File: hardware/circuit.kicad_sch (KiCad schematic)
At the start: 3 parts

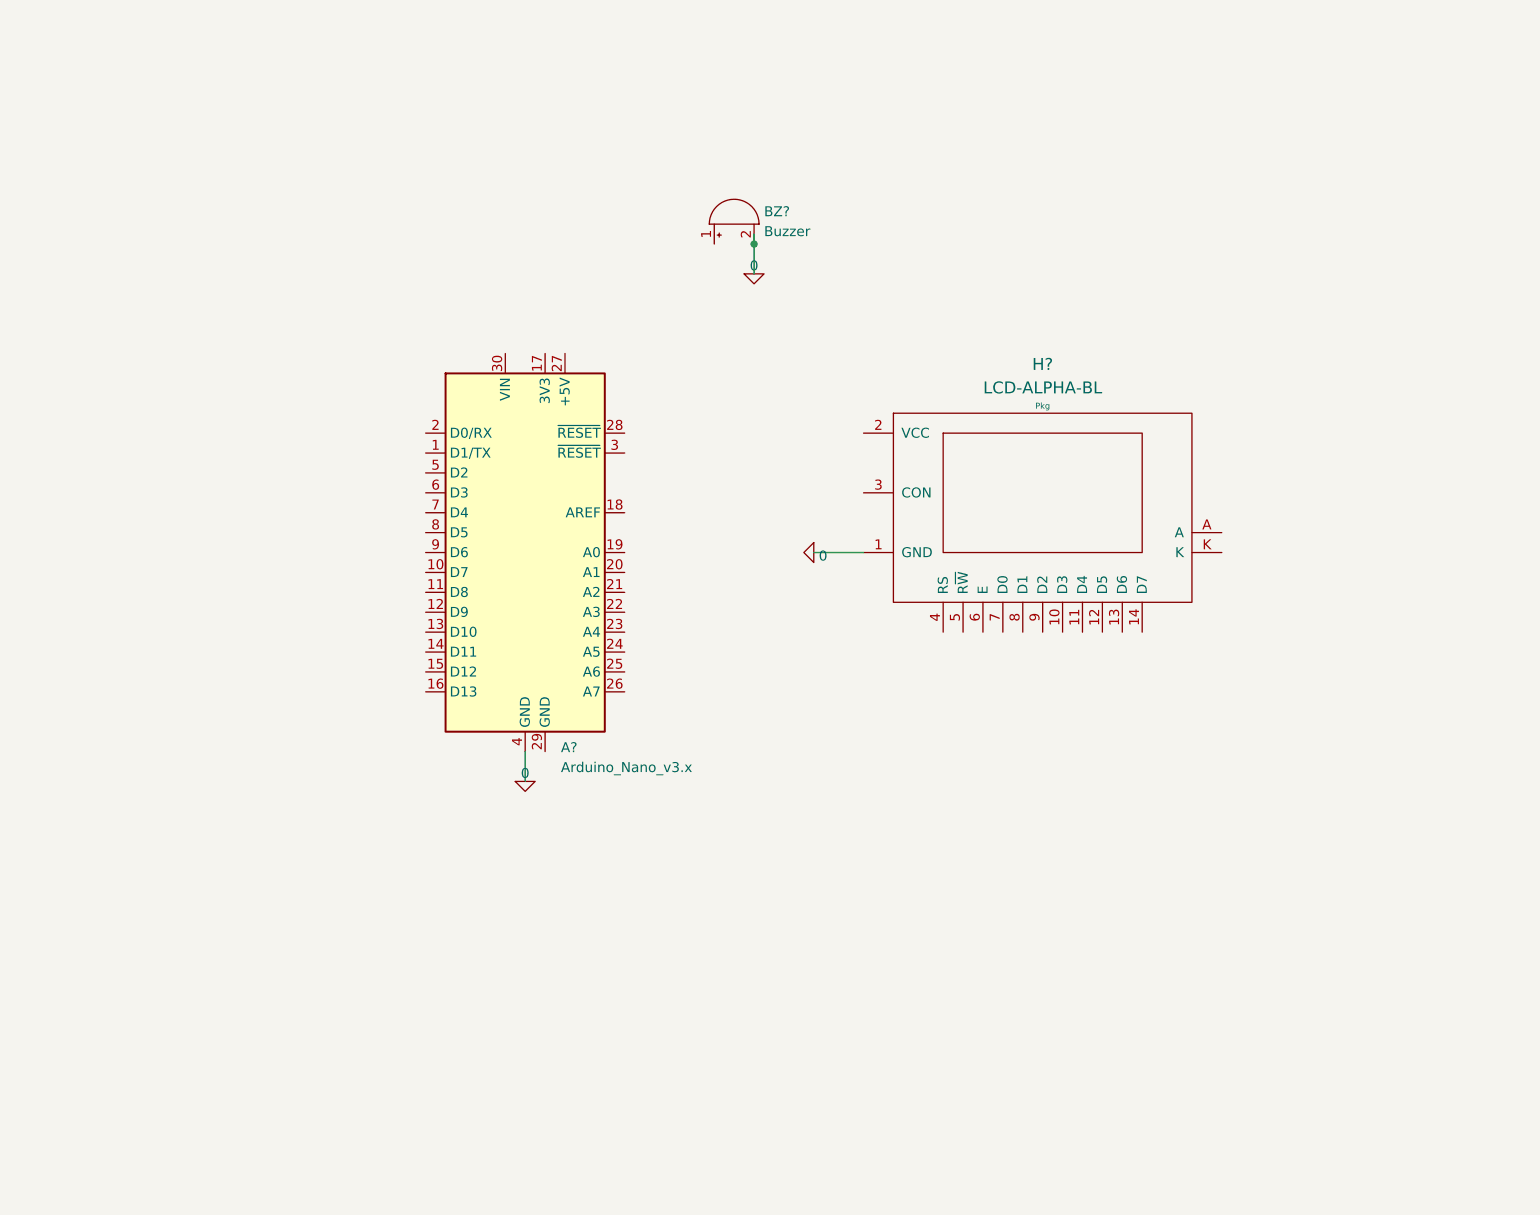
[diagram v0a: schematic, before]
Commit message: Added(guiMessage): generic lcd gui message functions
  Moved src/system/* to /, corrected some linting errors.
  Made some minor changes to hardware schematic.
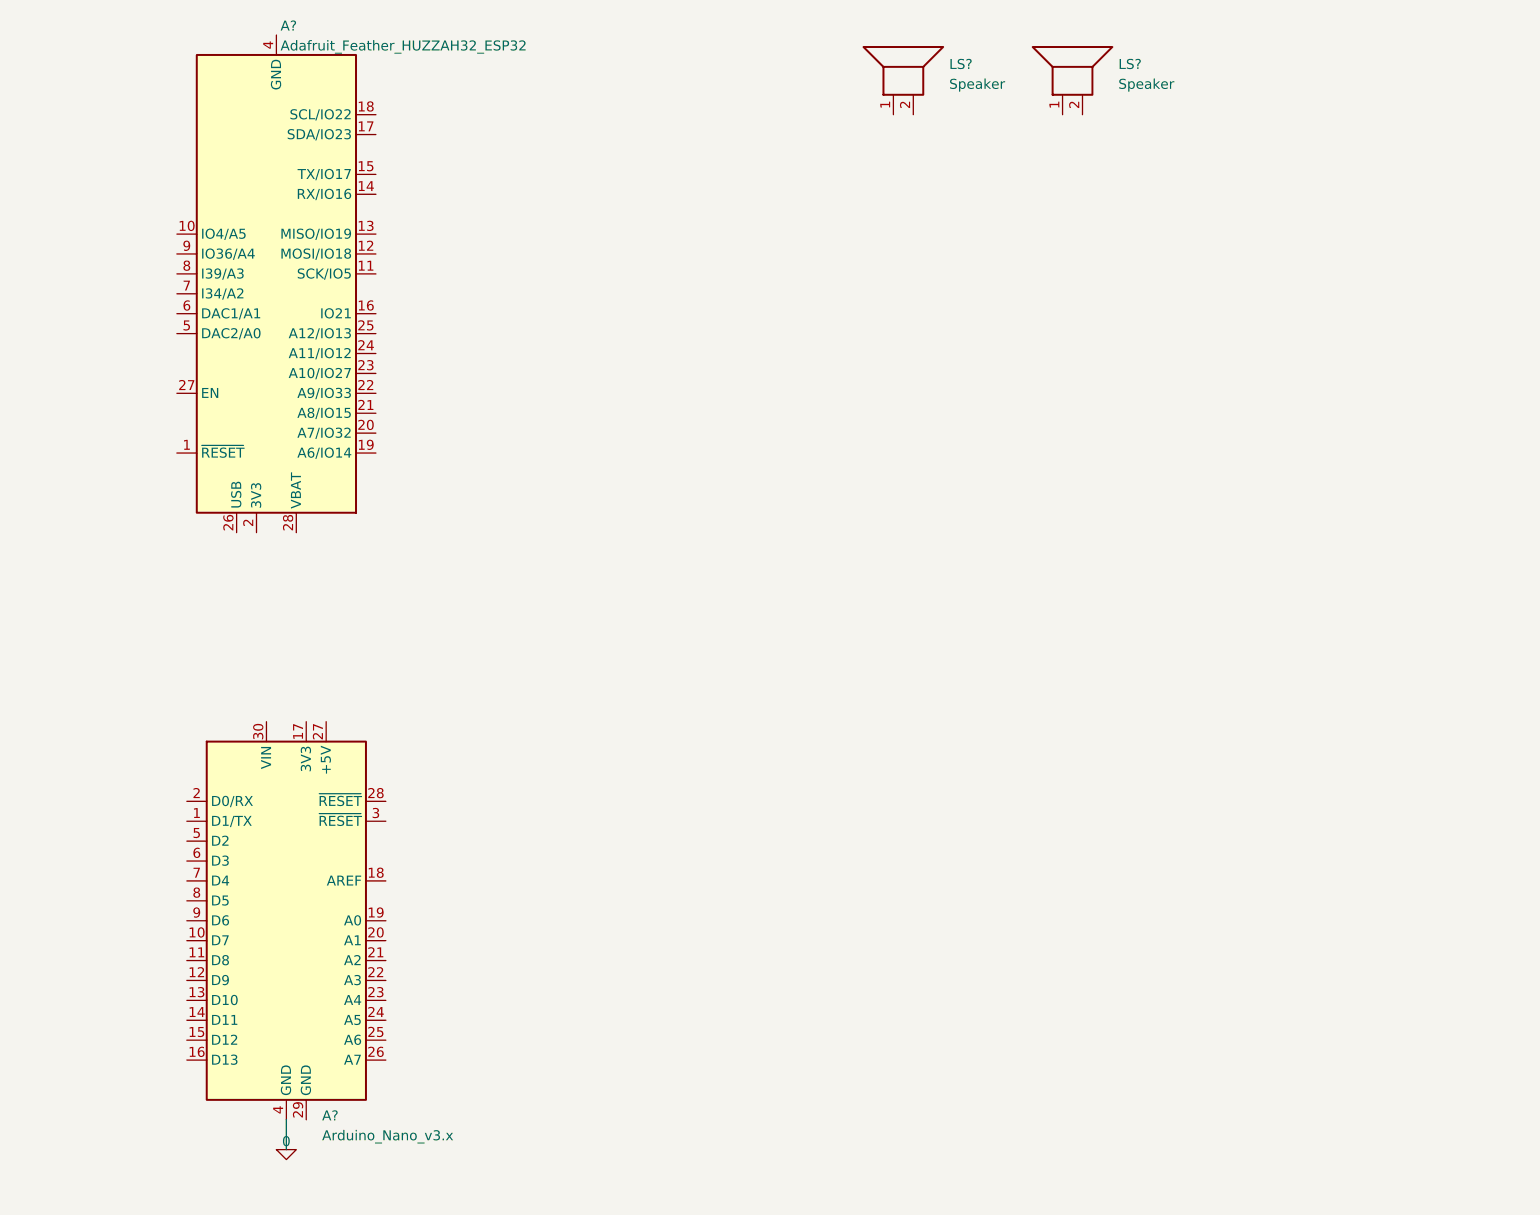
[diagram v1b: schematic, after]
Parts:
- removed BZ?: Buzzer, symbol Device:Buzzer
- removed H?: LCD-ALPHA-BL, Pkg, symbol display:LCD-ALPHA-BL
- added A?: Adafruit_Feather_HUZZAH32_ESP32, Module:Adafruit_Feather, symbol MCU_Module:Adafruit_Feather_HUZZAH32_ESP32
- added LS? (x2): Speaker, symbol Device:Speaker
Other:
- moved on the sheet: A?
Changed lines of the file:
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@@
 (kicad_sch (version 20211123) (generator eeschema)
   (paper "A4")
-  (junction (at 121.92 54.61) (diameter 0) (color 0 0 0 0)
-  )
-  (wire (pts (xy 121.92 53.34) (xy 121.92 54.61))
+  (wire (pts (xy 62.23 166.37) (xy 62.23 170.18))
     (stroke (width 0) (type default) (color 0 0 0 0))
   )
-  (wire (pts (xy 129.54 93.98) (xy 135.89 93.98))
-    (stroke (width 0) (type default) (color 0 0 0 0))
-  )
-  (wire (pts (xy 92.71 119.38) (xy 92.71 123.19))
-    (stroke (width 0) (type default) (color 0 0 0 0))
-  )
-  (wire (pts (xy 121.92 58.42) (xy 121.92 54.61))
-    (stroke (width 0) (type default) (color 0 0 0 0))
-  )
-  (symbol (lib_id "pspice:0") (at 129.54 93.98 270) (unit 1)
+  (symbol (lib_id "pspice:0") (at 62.23 170.18 0) (unit 1)
     (in_bom yes) (on_board yes) (fields_autoplaced)
-    (property "Reference" "#GND?" (id 0) (at 127 93.98 0)
+    (property "Reference" "#GND?" (id 0) (at 62.23 172.72 0)
       (effects (font (size 1.27 1.27)) hide)
     )
-    (property "Value" "0" (id 1) (at 130.175 94.4138 90)
-      (effects (font (size 1.27 1.27)) (justify left))
-    )
-    (property "Footprint" "" (id 2) (at 129.54 93.98 0)
+    (property "Value" "0" (id 1) (at 62.23 169.1442 0))
+    (property "Footprint" "" (id 2) (at 62.23 170.18 0)
       (effects (font (size 1.27 1.27)) hide)
     )
-    (property "Datasheet" "~" (id 3) (at 129.54 93.98 0)
+    (property "Datasheet" "~" (id 3) (at 62.23 170.18 0)
       (effects (font (size 1.27 1.27)) hide)
     )
     (pin "1")
   )
-  (symbol (lib_id "Device:Buzzer") (at 119.38 52.07 90) (unit 1)
+  (symbol (lib_id "MCU_Module:Adafruit_Feather_HUZZAH32_ESP32") (at 60.96 60.96 180) (unit 1)
     (in_bom yes) (on_board yes) (fields_autoplaced)
-    (property "Reference" "BZ?" (id 0) (at 123.19 50.4733 90)
+    (property "Reference" "A?" (id 0) (at 61.4806 26.7802 0)
       (effects (font (size 1.27 1.27)) (justify right))
     )
-    (property "Value" "Buzzer" (id 1) (at 123.19 53.0102 90)
+    (property "Value" "Adafruit_Feather_HUZZAH32_ESP32" (id 1) (at 61.4806 29.3171 0)
       (effects (font (size 1.27 1.27)) (justify right))
     )
-    (property "Footprint" "" (id 2) (at 116.84 52.705 90)
+    (property "Footprint" "Module:Adafruit_Feather" (id 2) (at 58.42 26.67 0)
+      (effects (font (size 1.27 1.27)) (justify left) hide)
+    )
+    (property "Datasheet" "https://cdn-learn.adafruit.com/downloads/pdf/adafruit-huzzah32-esp32-feather.pdf" (id 3) (at 60.96 30.48 0)
       (effects (font (size 1.27 1.27)) hide)
     )
-    (property "Datasheet" "~" (id 3) (at 116.84 52.705 90)
-      (effects (font (size 1.27 1.27)) hide)
-    )
-    (pin "1")
-    (pin "2")
-  )
-  (symbol (lib_id "pspice:0") (at 92.71 123.19 0) (unit 1)
-    (in_bom yes) (on_board yes) (fields_autoplaced)
-    (property "Reference" "#GND?" (id 0) (at 92.71 125.73 0)
-      (effects (font (size 1.27 1.27)) hide)
-    )
-    (property "Value" "0" (id 1) (at 92.71 122.1542 0))
-    (property "Footprint" "" (id 2) (at 92.71 123.19 0)
-      (effects (font (size 1.27 1.27)) hide)
-    )
-    (property "Datasheet" "~" (id 3) (at 92.71 123.19 0)
-      (effects (font (size 1.27 1.27)) hide)
-    )
-    (pin "1")
-  )
-  (symbol (lib_id "pspice:0") (at 121.92 58.42 0) (unit 1)
-    (in_bom yes) (on_board yes) (fields_autoplaced)
-    (property "Reference" "#GND?" (id 0) (at 121.92 60.96 0)
-      (effects (font (size 1.27 1.27)) hide)
-    )
-    (property "Value" "0" (id 1) (at 121.92 57.3842 0))
-    (property "Footprint" "" (id 2) (at 121.92 58.42 0)
-      (effects (font (size 1.27 1.27)) hide)
-    )
-    (property "Datasheet" "~" (id 3) (at 121.92 58.42 0)
-      (effects (font (size 1.27 1.27)) hide)
-    )
-    (pin "1")
-  )
-  (symbol (lib_id "display:LCD-ALPHA-BL") (at 158.75 86.36 0) (unit 1)
-    (in_bom yes) (on_board yes) (fields_autoplaced)
-    (property "Reference" "H?" (id 0) (at 158.75 69.9717 0)
-      (effects (font (size 1.524 1.524)))
-    )
-    (property "Value" "LCD-ALPHA-BL" (id 1) (at 158.75 72.9651 0)
-      (effects (font (size 1.524 1.524)))
-    )
-    (property "Footprint" "Pkg" (id 2) (at 158.75 75.2737 0)
-      (effects (font (size 0.762 0.762)))
-    )
-    (property "Datasheet" "" (id 3) (at 158.75 86.36 0))
     (pin "1")
     (pin "10")
@@
     (pin "13")
     (pin "14")
+    (pin "15")
+    (pin "16")
+    (pin "17")
+    (pin "18")
+    (pin "19")
     (pin "2")
+    (pin "20")
+    (pin "21")
+    (pin "22")
+    (pin "23")
+    (pin "24")
+    (pin "25")
+    (pin "26")
+    (pin "27")
+    (pin "28")
     (pin "3")
     (pin "4")
@@
     (pin "8")
     (pin "9")
-    (pin "A")
-    (pin "K")
   )
-  (symbol (lib_id "MCU_Module:Arduino_Nano_v3.x") (at 92.71 93.98 0) (unit 1)
+  (symbol (lib_id "Device:Speaker") (at 161.29 33.02 90) (unit 1)
     (in_bom yes) (on_board yes) (fields_autoplaced)
-    (property "Reference" "A?" (id 0) (at 97.2694 118.8704 0)
+    (property "Reference" "LS?" (id 0) (at 168.402 31.6773 90)
+      (effects (font (size 1.27 1.27)) (justify right))
+    )
+    (property "Value" "Speaker" (id 1) (at 168.402 34.2142 90)
+      (effects (font (size 1.27 1.27)) (justify right))
+    )
+    (property "Footprint" "" (id 2) (at 166.37 33.02 0)
+      (effects (font (size 1.27 1.27)) hide)
+    )
+    (property "Datasheet" "~" (id 3) (at 162.56 33.274 0)
+      (effects (font (size 1.27 1.27)) hide)
+    )
+    (pin "1")
+    (pin "2")
+  )
+  (symbol (lib_id "MCU_Module:Arduino_Nano_v3.x") (at 62.23 140.97 0) (unit 1)
+    (in_bom yes) (on_board yes) (fields_autoplaced)
+    (property "Reference" "A?" (id 0) (at 66.7894 165.8604 0)
       (effects (font (size 1.27 1.27)) (justify left))
     )
-    (property "Value" "Arduino_Nano_v3.x" (id 1) (at 97.2694 121.4073 0)
+    (property "Value" "Arduino_Nano_v3.x" (id 1) (at 66.7894 168.3973 0)
       (effects (font (size 1.27 1.27)) (justify left))
     )
-    (property "Footprint" "Module:Arduino_Nano" (id 2) (at 92.71 93.98 0)
+    (property "Footprint" "Module:Arduino_Nano" (id 2) (at 62.23 140.97 0)
       (effects (font (size 1.27 1.27) italic) hide)
     )
-    (property "Datasheet" "http://www.mouser.com/pdfdocs/Gravitech_Arduino_Nano3_0.pdf" (id 3) (at 92.71 93.98 0)
+    (property "Datasheet" "http://www.mouser.com/pdfdocs/Gravitech_Arduino_Nano3_0.pdf" (id 3) (at 62.23 140.97 0)
       (effects (font (size 1.27 1.27)) hide)
     )
@@
     (pin "9")
   )
+  (symbol (lib_id "Device:Speaker") (at 139.7 33.02 90) (unit 1)
+    (in_bom yes) (on_board yes) (fields_autoplaced)
+    (property "Reference" "LS?" (id 0) (at 146.812 31.6773 90)
+      (effects (font (size 1.27 1.27)) (justify right))
+    )
+    (property "Value" "Speaker" (id 1) (at 146.812 34.2142 90)
+      (effects (font (size 1.27 1.27)) (justify right))
+    )
+    (property "Footprint" "" (id 2) (at 144.78 33.02 0)
+      (effects (font (size 1.27 1.27)) hide)
+    )
+    (property "Datasheet" "~" (id 3) (at 140.97 33.274 0)
+      (effects (font (size 1.27 1.27)) hide)
+    )
+    (pin "1")
+    (pin "2")
+  )
   (sheet_instances
     (path "/" (page "1"))
   )
   (symbol_instances
-    (path "/0bb73dc6-7cf1-4496-ade7-f779f1058461"
-      (reference "#GND?") (unit 1) (value "0") (footprint "")
-    )
     (path "/6bebfc03-0fe0-49ee-98c1-28bf41e38a1a"
       (reference "#GND?") (unit 1) (value "0") (footprint "")
     )
-    (path "/bfc94fbe-5bae-4a0f-92a0-3549e2861131"
-      (reference "#GND?") (unit 1) (value "0") (footprint "")
+    (path "/7460f81c-279a-4371-92da-be5818d3a9aa"
+      (reference "A?") (unit 1) (value "Adafruit_Feather_HUZZAH32_ESP32") (footprint "Module:Adafruit_Feather")
     )
     (path "/df182eb9-d262-431a-a684-628d6e8fa699"
       (reference "A?") (unit 1) (value "Arduino_Nano_v3.x") (footprint "Module:Arduino_Nano")
     )
-    (path "/3e68c2ca-29e8-4fe0-b52c-b9b36a433edc"
-      (reference "BZ?") (unit 1) (value "Buzzer") (footprint "")
+    (path "/c591a9ec-7514-4ae2-92ae-b82494b55aff"
+      (reference "LS?") (unit 1) (value "Speaker") (footprint "")
     )
-    (path "/c72dc957-0bd4-472b-93aa-6b844cbab5d9"
-      (reference "H?") (unit 1) (value "LCD-ALPHA-BL") (footprint "Pkg")
+    (path "/f9bdadf6-6ed8-4afd-b3ae-b3c887040cb0"
+      (reference "LS?") (unit 1) (value "Speaker") (footprint "")
     )
   )

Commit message: Update(hardware): Updated hardware schematic for documentation
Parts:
- added BZ1: Buzzer, symbol Device:Buzzer
- added R1, R2: 2200, symbol Device:R
- added R3, R4: 1000, symbol Device:R
- added R5: 100k, symbol Device:R_Potentiometer_Trim
- added R6, R7, R8, R9: 4700, symbol Device:R
- added SW? (x16): SW_DPST_x2, symbol Switch:SW_DPST_x2
- added SW?: SW_DIP_x04, symbol Switch:SW_DIP_x04
- added U?: EA_T123X-I2C, Display:EA_T123X-I2C, symbol Display_Character:EA_T123X-I2C
- added U?: WeMos_D1_mini, Module:WEMOS_D1_mini_light, symbol MCU_Module:WeMos_D1_mini
- gave numbers to parts that had none: 2
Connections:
- net 0: now also A?.29 (GND)
- net at A?.14 (RX/IO16): now also R2.1, R4.2
- net at A?.15 (TX/IO17): now also R1.1, R3.2
- net at A?.18 (SCL/IO22): now also R5.3
- net V3.3: now reaches A?.2 (3V3)
- net V3.3: now also A?.17 (3V3)
- net GND: now reaches A?.4 (GND)
- net GND: now also LS2.2, BZ1.2 (+), R1.2, R2.2, R5.1, R6.1, R7.1, R8.1, R9.1, U?.10 (GND)
- net at LS2.1: now also LS1.2
- net TX: now reaches A?.1 (D1/TX)
- net TX: now also SW?.1
- net Min4: now reaches A?.10 (D7)
- net Min4: now also R9.2
- net BuzIn: now reaches A?.11 (D8)
- net BuzIn: now also BZ1.1 (-)
- net Mout1: now reaches A?.19 (A0)
- net RX: now reaches A?.2 (D0/RX)
- net RX: now also SW?.2
- net Mout2: now reaches A?.20 (A1)
- net Mout3: now reaches A?.21 (A2)
- net Mout4: now reaches A?.22 (A3)
- net Vin: now reaches A?.30 (VIN)
- net Vin: now also U?.9 (5V)
- net sigAlarm: now reaches A?.5 (D2)
- net sigAlarm: now also U?.4 (SCK/D5)
- net Min1: now reaches A?.7 (D4)
- net Min1: now also R7.2
- net Min2: now reaches A?.8 (D5)
- net Min2: now also R6.2
- net Min3: now reaches A?.9 (D6)
- net Min3: now also R8.2
- net sigAudio: now reaches LS1.1
- new net: R3.1, SW?.7
- new net: R4.1, SW?.8
- new net I2S_Voice: R5.2
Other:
- moved on the sheet: A?, LS1, LS2
